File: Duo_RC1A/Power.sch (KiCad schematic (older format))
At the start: 21 parts, among them U2 MC7805

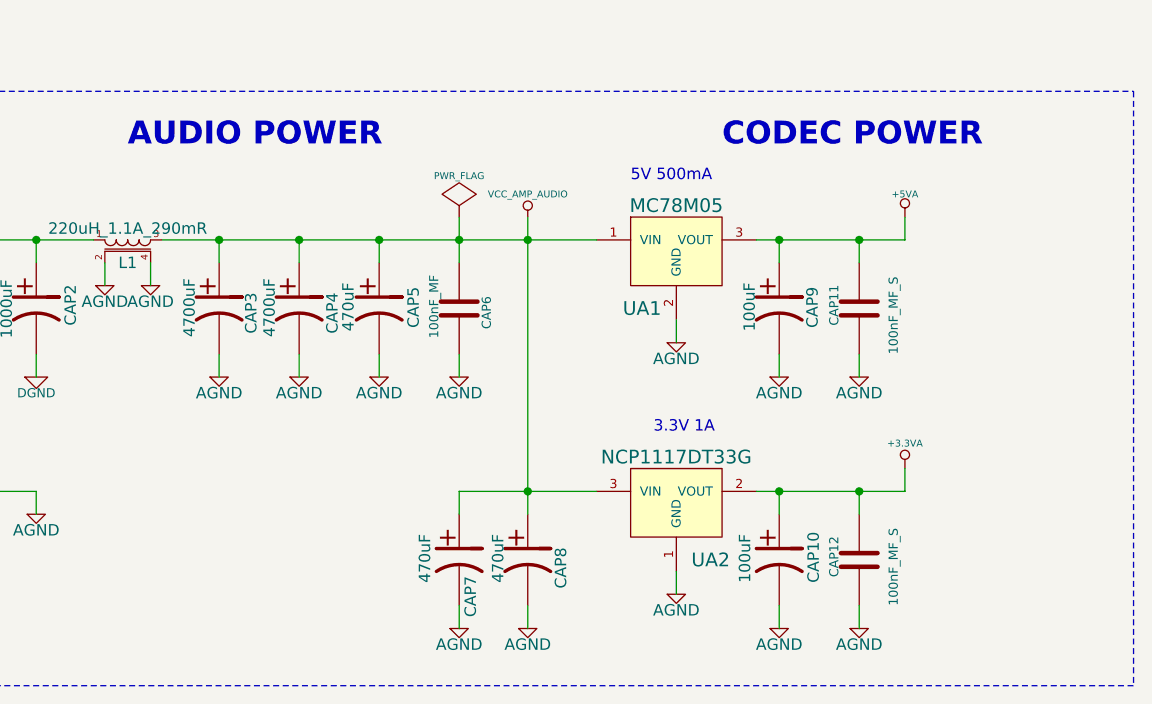
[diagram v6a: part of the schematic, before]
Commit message: Finalized the audio input, output and headphone. Changing the CODEC placement.
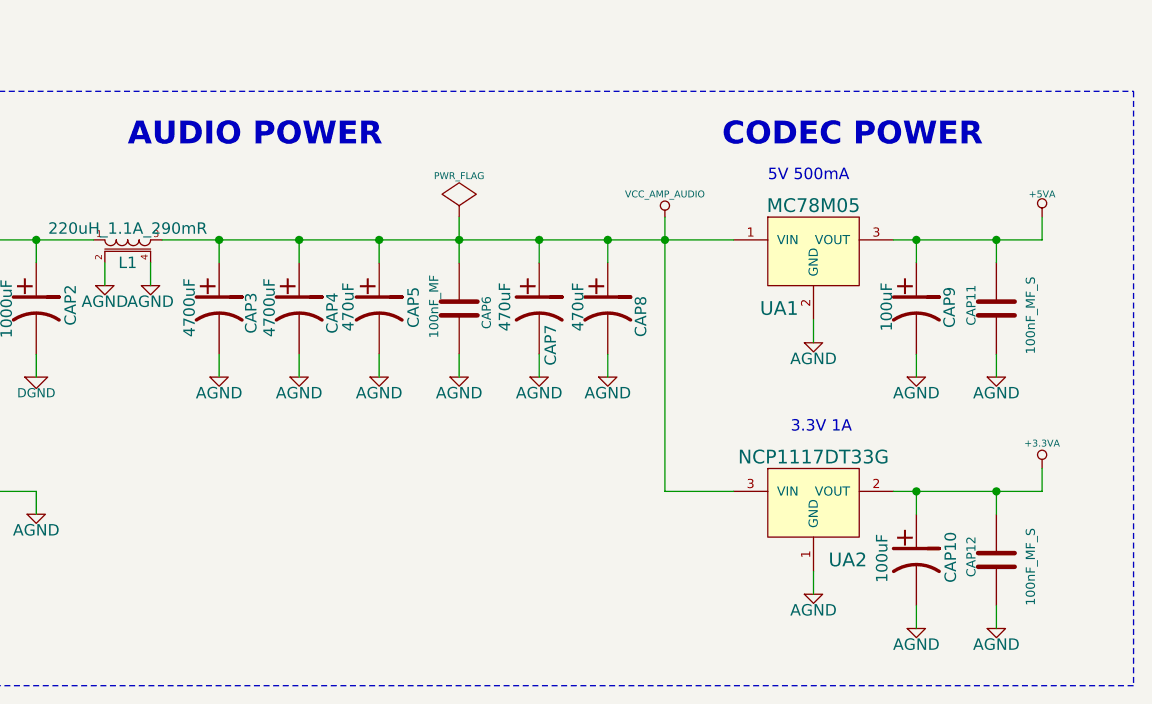
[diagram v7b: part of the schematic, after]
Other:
- moved on the sheet: CAP10, CAP11, CAP12, CAP7, CAP8, CAP9, UA1, UA2

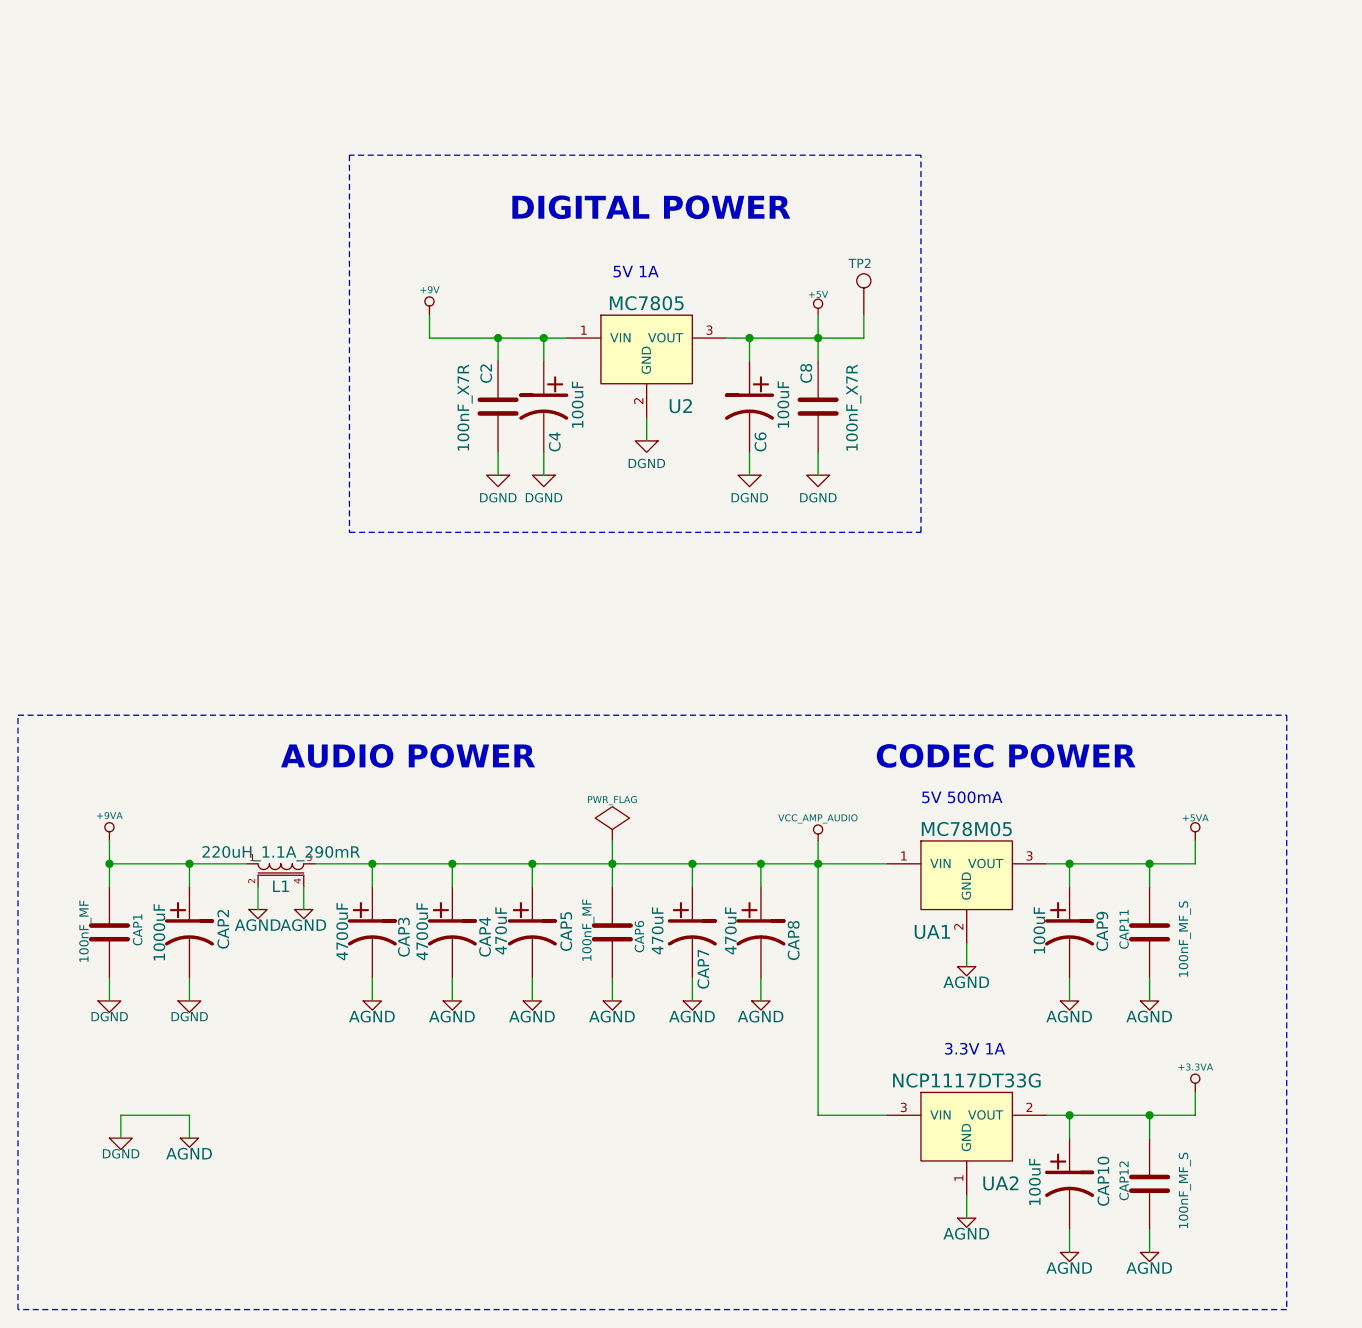
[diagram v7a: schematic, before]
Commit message: Starting to implement new ground topology.
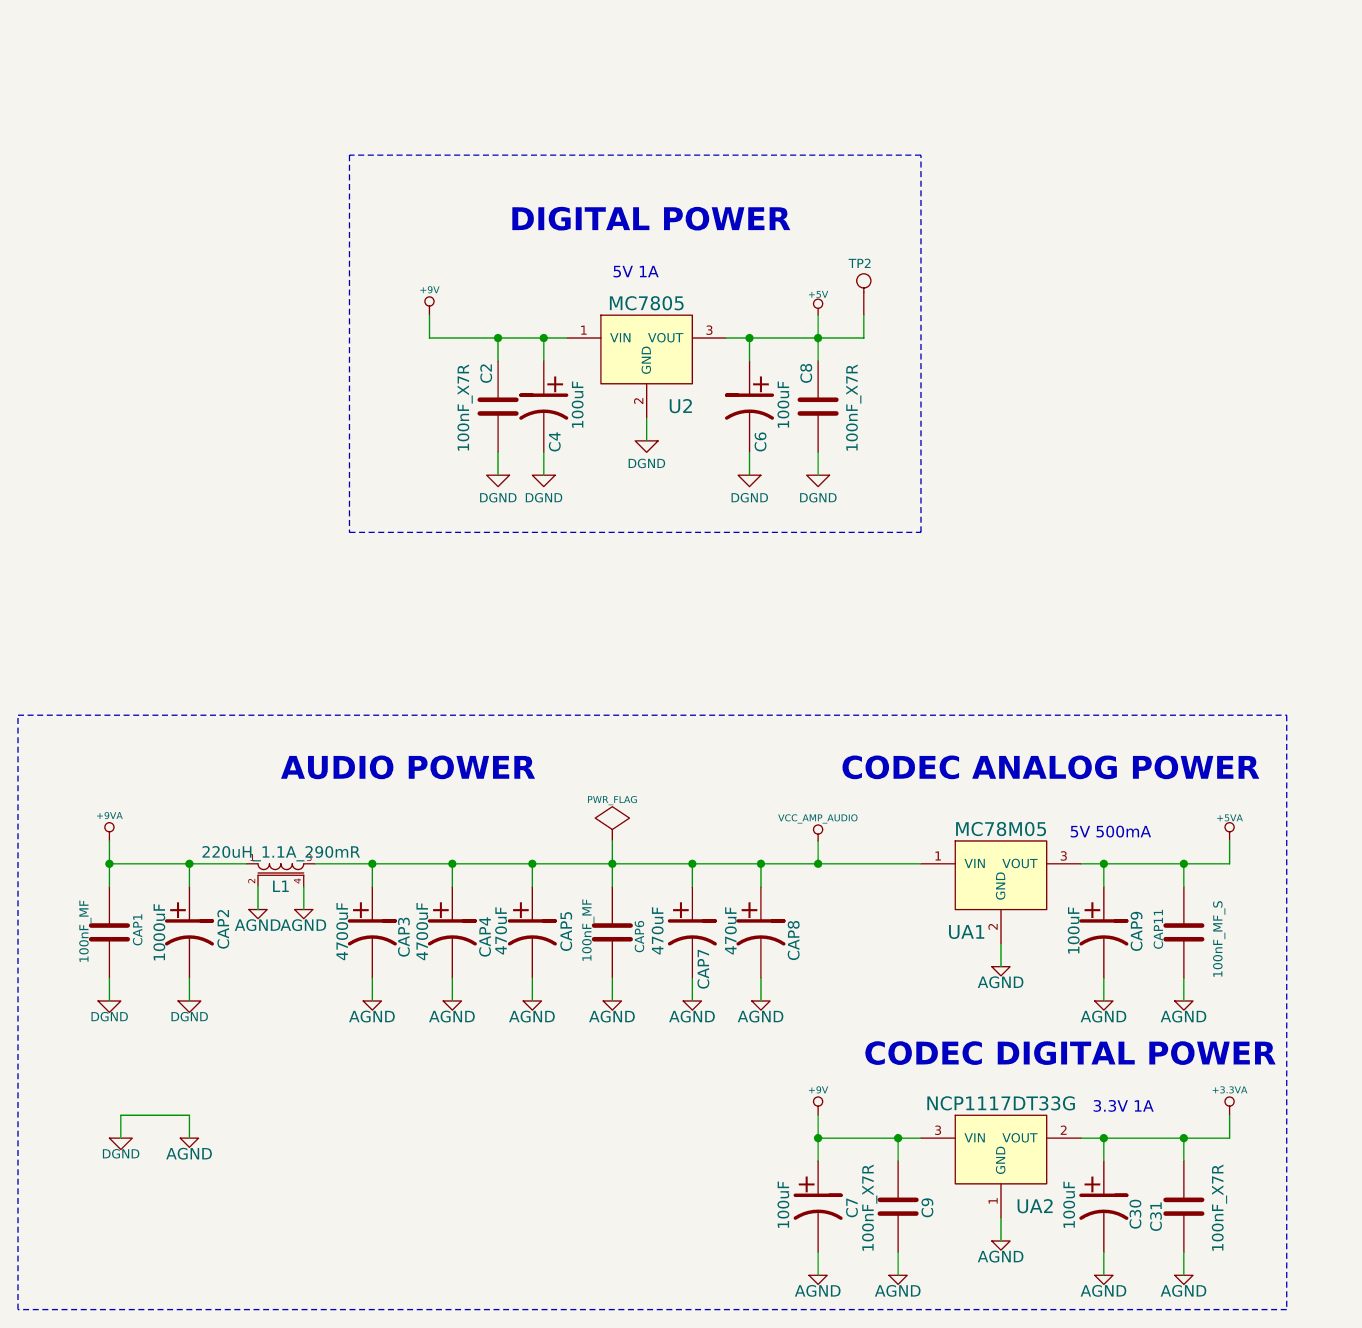
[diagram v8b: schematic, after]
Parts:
- removed CAP12: 100nF_MF_S, Duo_Audio_HMI_RC1A:CapacitorMetalFilm_7.2x2.5MM_P5MM, symbol C
- added C31, C9: 100nF_X7R, Duo_Audio_HMI_RC1A:SM0603, symbol C
- added C7: 100uF, Duo_Audio_HMI_RC1A:Capacitor5x11RM2, symbol CP1
- renumbered CAP10 to C30
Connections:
- net +3.3VA: now also C31.1
- net +9V: now also UA2.3 (VIN), C7.1, C9.1
- net AGND: now also C31.2, C7.2, C9.2
- net VCC_AMP_AUDIO: no longer UA2.3 (VIN)
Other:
- note added: "CODEC ANALOG POWER"
- note added: "CODEC DIGITAL POWER"
- note removed: "CODEC POWER"
- moved on the sheet: C30, CAP11, CAP9, UA1, UA2
